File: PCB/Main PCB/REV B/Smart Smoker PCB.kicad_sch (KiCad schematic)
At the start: 72 parts, among them J1 393570002, J2 MJ-3502, J3 1051330001, J4 MJ-3502, J5 MJ-3502, J6 MJ-3502, J7 Hopper, J8 Micro_SD_Card_Det, J9 Lid, Q1 25V 1.5A Trans, Q2 25V 1.5A Trans, U1 ESP32-WROOM-32UE_16MB, U2 DG409LEDY-T1-GE3, U3 MAX31855KASA, U4 CP2102N-Axx-xQFN20

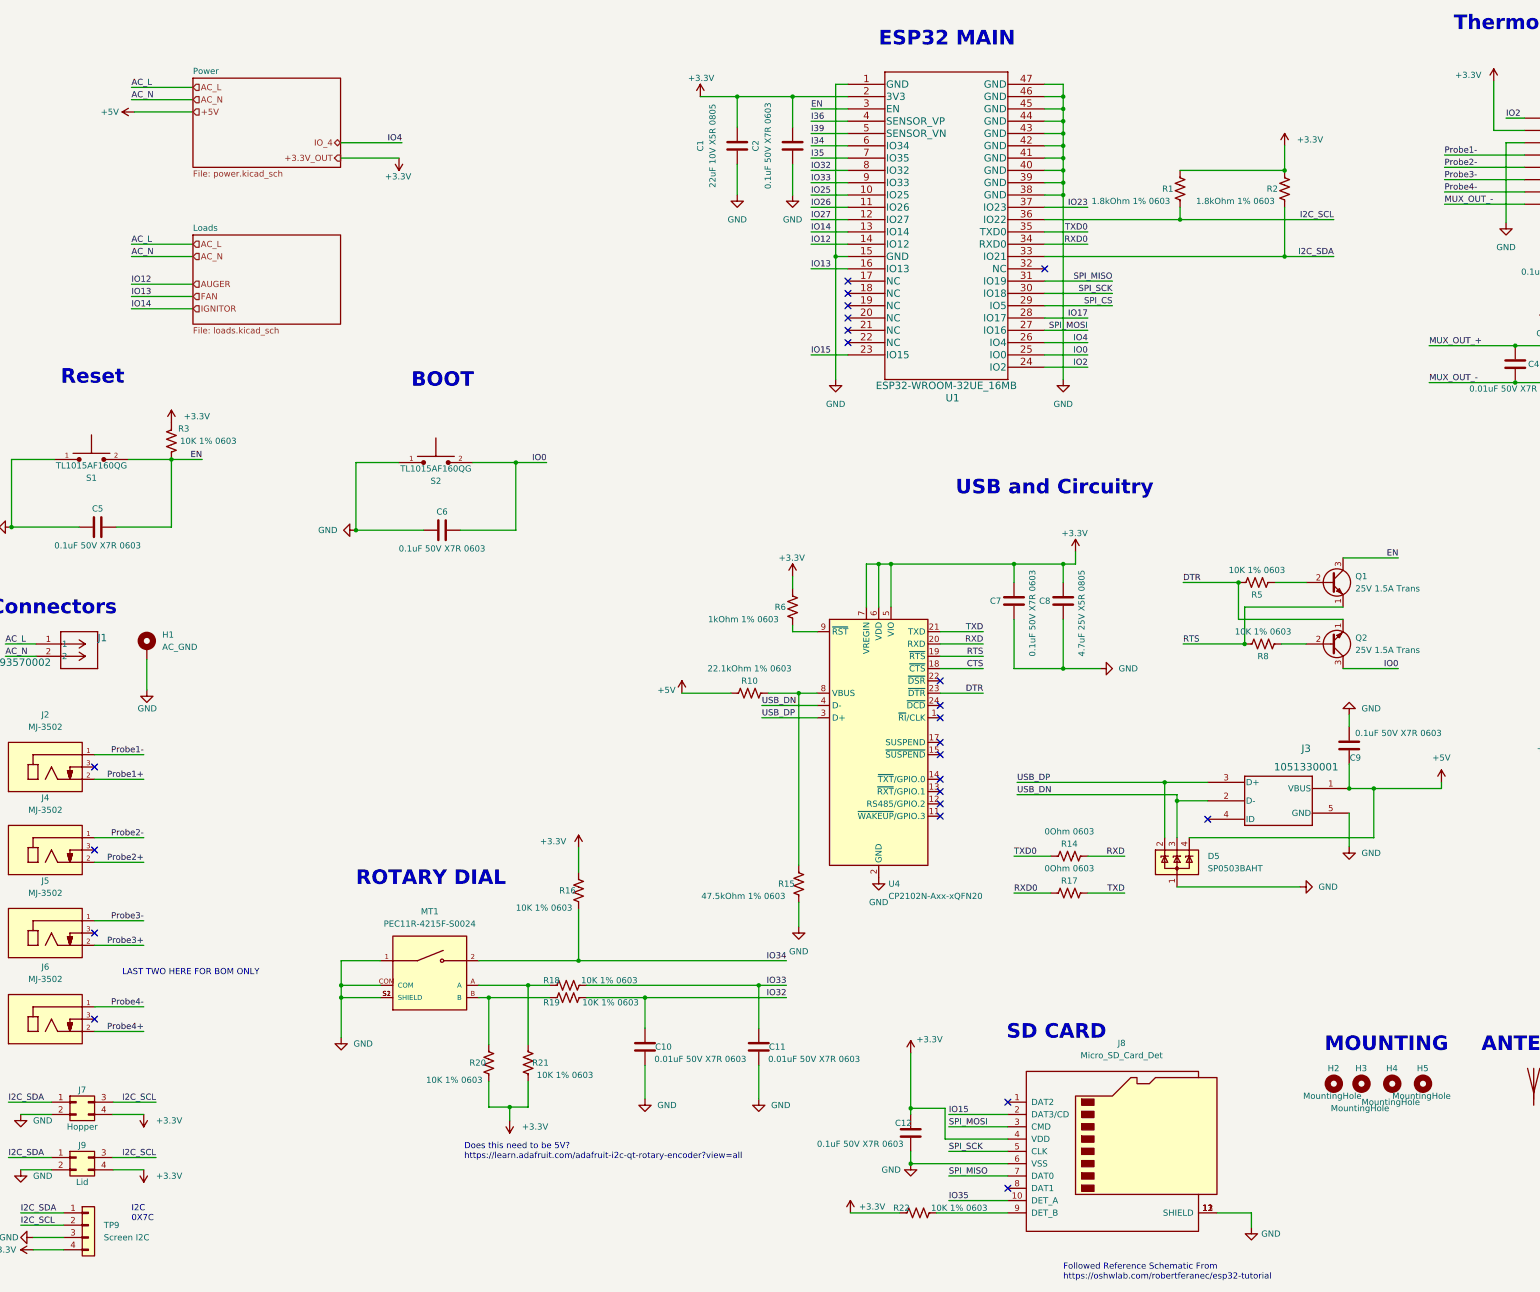
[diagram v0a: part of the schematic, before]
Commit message: PCB schematic updates, added 5V power supply
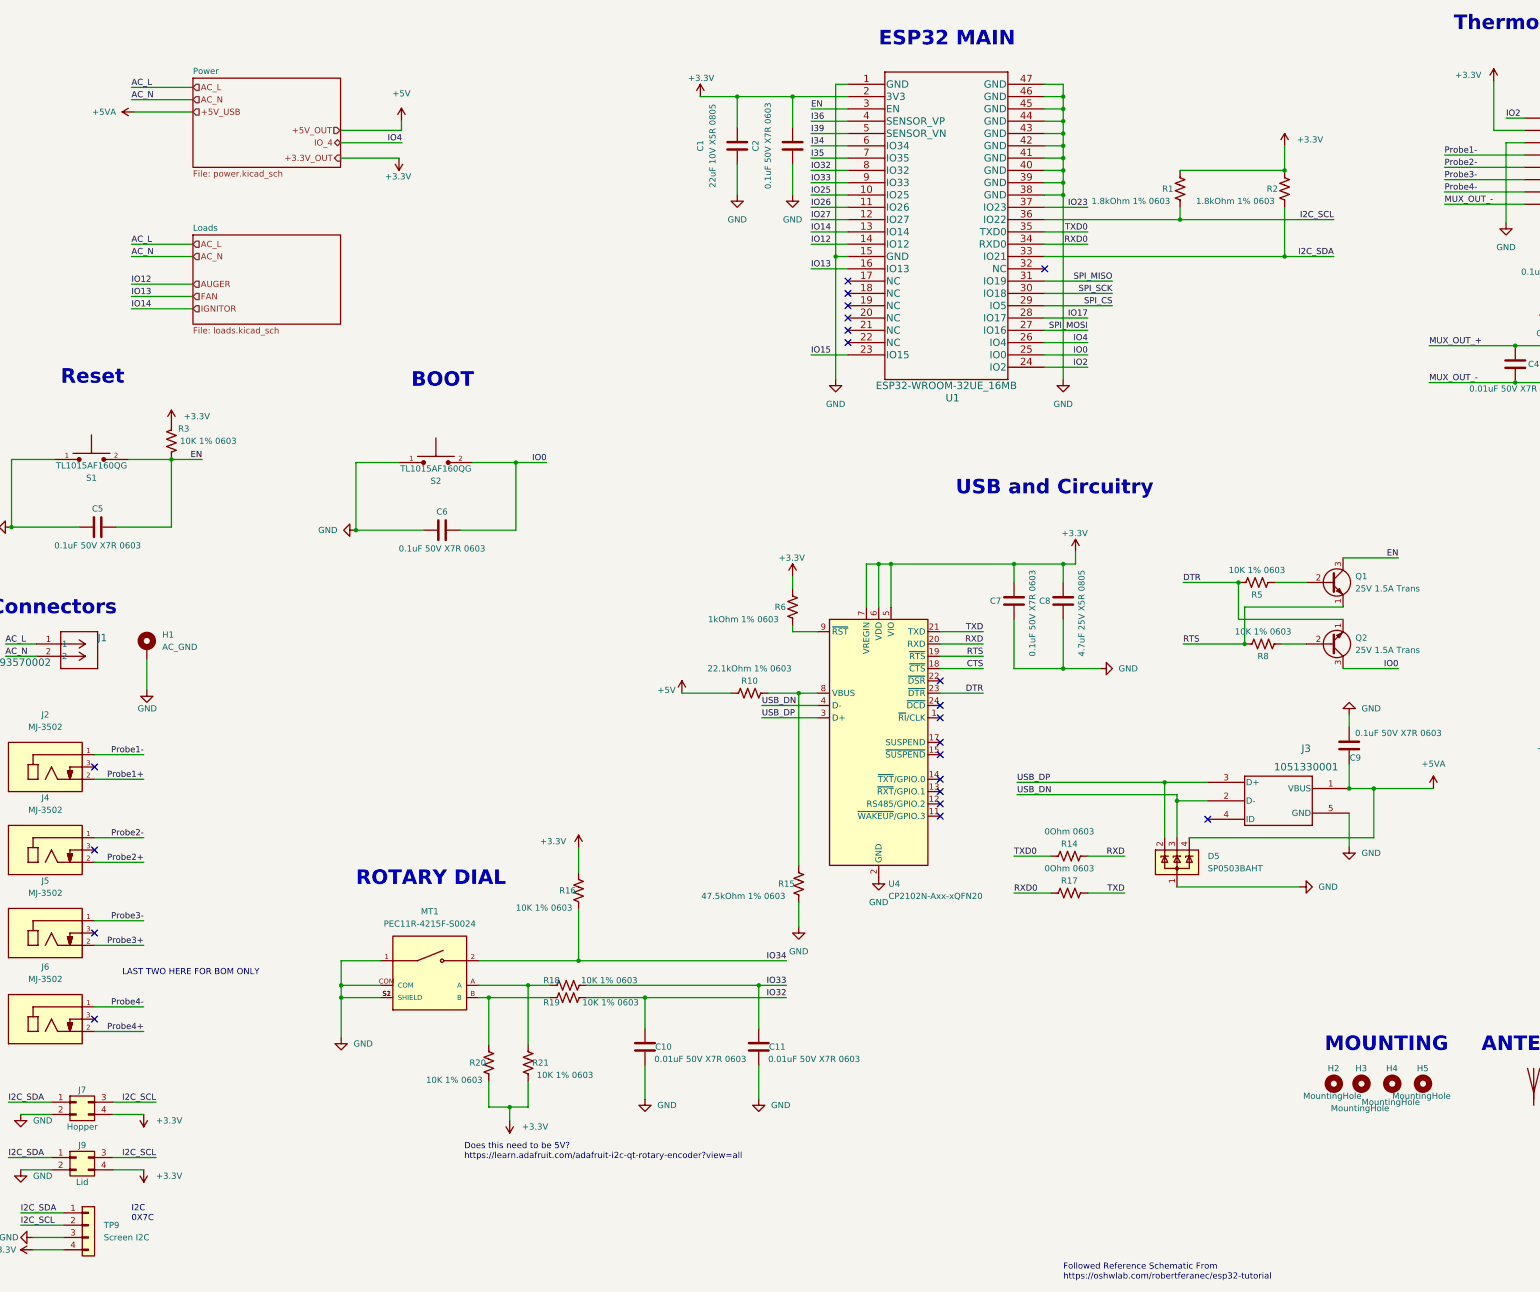
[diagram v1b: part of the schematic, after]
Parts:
- removed C12: 0.1uF 50V X7R 0603, Capacitor_SMD:C_0603_1608Metric, symbol Device:C
- removed J8: Micro_SD_Card_Det, Customs Smoker:DM3CS-SF_HIR, symbol Connector:Micro_SD_Card_Det
- removed R22: 10K 1% 0603, Resistor_SMD:R_0603_1608Metric, symbol Device:R_US
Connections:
- net +5V: no longer C9.1, D5.4 (K), J3.1 (VBUS)
- new net +5VA: C9.1, D5.4 (K), J3.1 (VBUS)
- no-connect marks 23 -> 21
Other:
- note removed: "SD CARD"

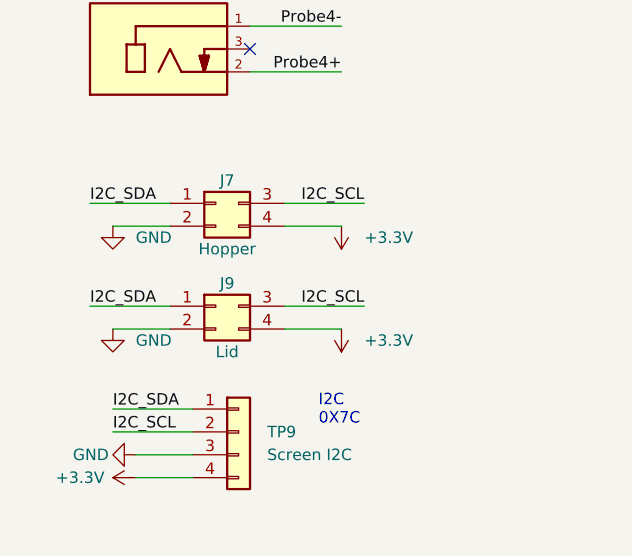
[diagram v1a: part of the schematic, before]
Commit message: PCB schematic updates, Modified and fixed all power sheets
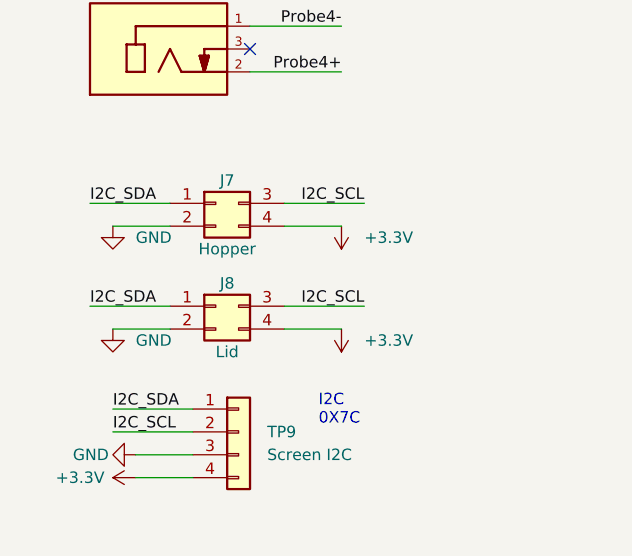
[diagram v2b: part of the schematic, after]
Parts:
- renumbered J9 to J8

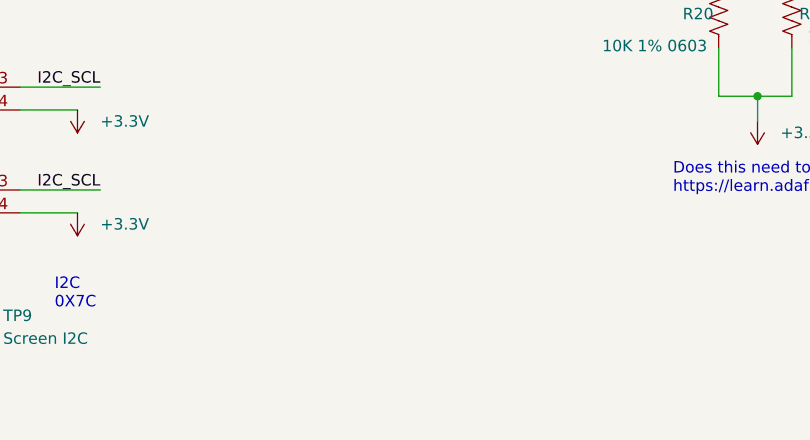
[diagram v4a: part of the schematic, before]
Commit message: PCB schematic updates, Relay Circuits Completed
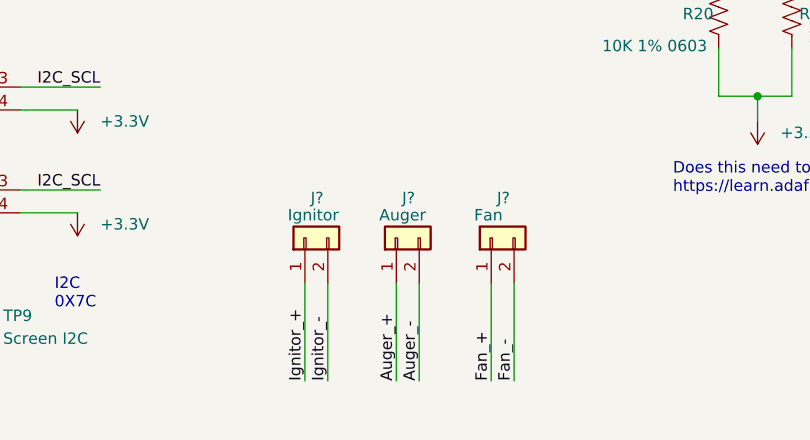
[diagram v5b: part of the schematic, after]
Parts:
- added J?: Fan, TestPoint:TestPoint_2Pads_Pitch5.08mm_Drill1.3mm, symbol Connector_Generic:Conn_01x02
- added J?: Ignitor, TestPoint:TestPoint_2Pads_Pitch5.08mm_Drill1.3mm, symbol Connector_Generic:Conn_01x02
- added J?: Auger, TestPoint:TestPoint_2Pads_Pitch5.08mm_Drill1.3mm, symbol Connector_Generic:Conn_01x02
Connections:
- new net Auger_+: J?.1 (Pin_1)
- new net Auger_-: J?.2 (Pin_2)
- new net Fan_+: J?.1 (Pin_1)
- new net Fan_-: J?.2 (Pin_2)
- new net Ignitor_+: J?.1 (Pin_1)
- new net Ignitor_-: J?.2 (Pin_2)

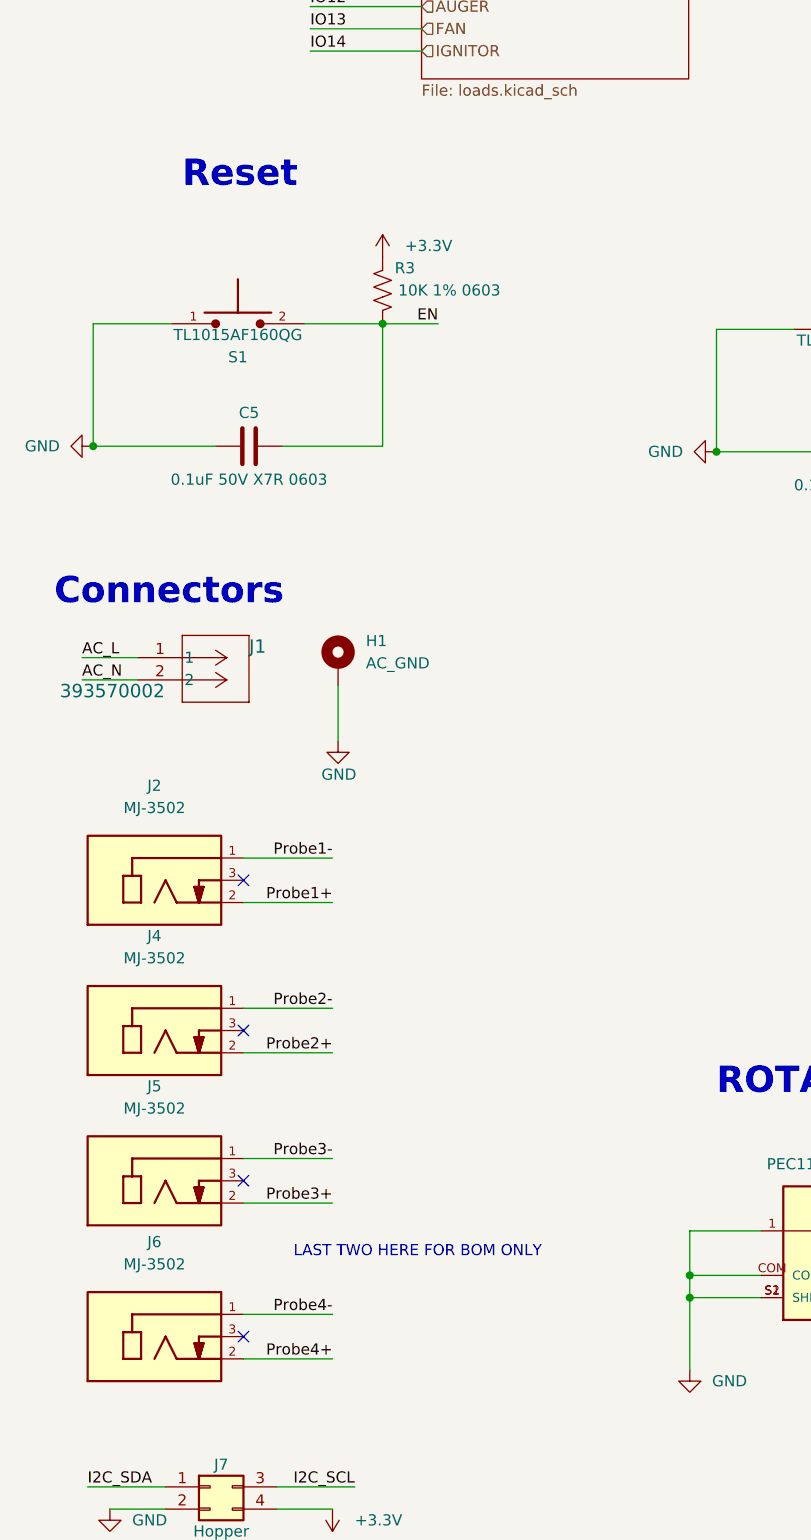
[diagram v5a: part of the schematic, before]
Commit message: PCB schematic updates, Thermocouple connector sourced and updated
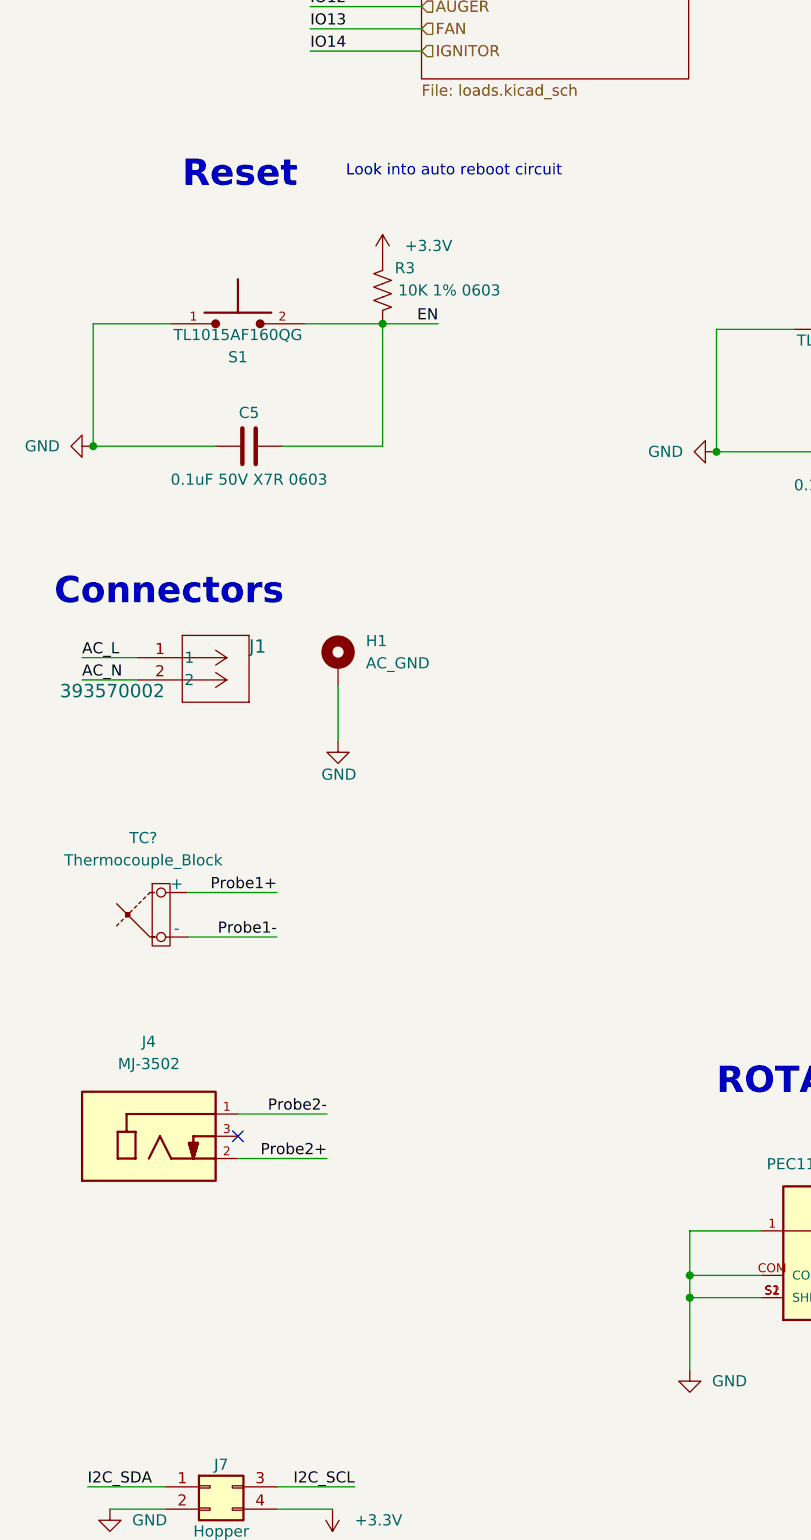
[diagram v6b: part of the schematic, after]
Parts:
- removed J2: MJ-3502, Customs Smoker:CUI_MJ-3502, symbol MJ-3502:MJ-3502
- removed J5, J6: MJ-3502, TestPoint:TestPoint_2Pads_Pitch5.08mm_Drill1.3mm, symbol MJ-3502:MJ-3502
- added TC?: Thermocouple_Block, Customs Smoker:K-TypeAdapter, symbol Device:Thermocouple_Block
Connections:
- net Probe1+: now also TC?.1 (+)
- net Probe1-: now also TC?.2 (-)
- no-connect marks 21 -> 18
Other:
- note added: "Look into auto reboot circuit"
- note removed: "LAST TWO HERE FOR BOM ONLY"
- moved on the sheet: J4
